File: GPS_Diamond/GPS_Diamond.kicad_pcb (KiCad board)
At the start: 4 copper layers, 20 x 20 mm, 36 parts, among them J1 CONN_01X04_MALE, J2 TEST_1P, J3 TEST_1P, J5 TEST_1P, J6 TEST_1P, U1 TCR2LE33LM, U2 STM32F042K6Ux, U3 SAM-M8Q, U4 FXOS8700CQ, U5 MS5637

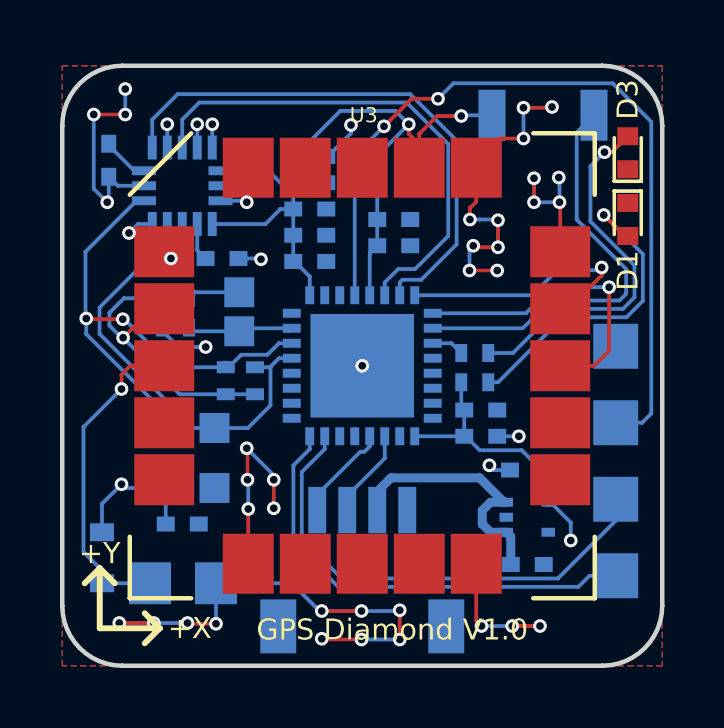
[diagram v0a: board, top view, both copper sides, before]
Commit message: Changed the boot0 jumper to a button and rearanged the baro.
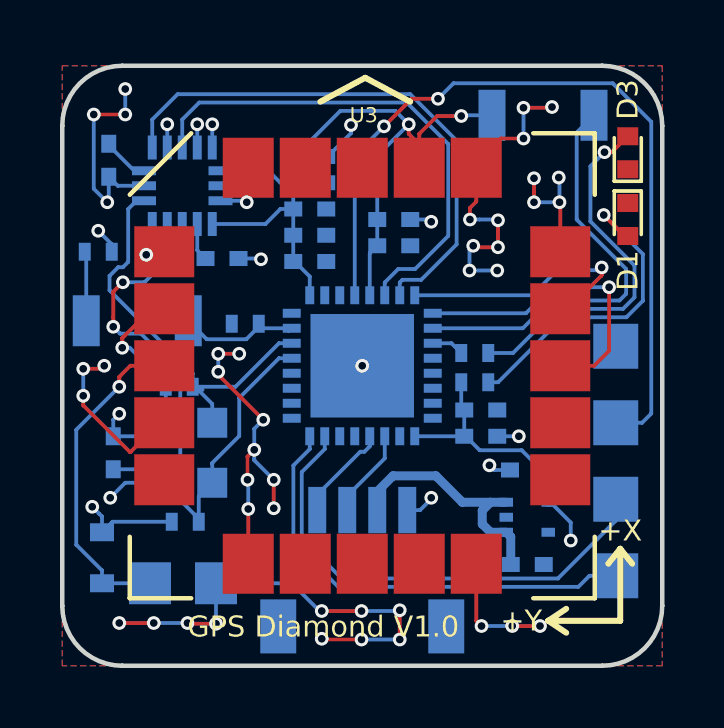
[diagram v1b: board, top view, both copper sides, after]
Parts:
- B1: footprint jumper:SOLDER-JUMPER_1-WAY -> Buttons_Switches_SMD:SW_SPST_B3U-1000P
- moved R6 5.24 mm to (144.1, 105.2), turned to 180 degrees
- moved B1 3.41 mm to (142.5, 98.5), turned to 0 degrees
- moved C11 3.31 mm to (141.7, 102.9), turned to 270 degrees
- moved R1 3.01 mm to (141.2, 96.2), turned to 180 degrees
- moved R7 2.33 mm to (146.1, 98.6)
- moved R8 1.56 mm to (143.9, 100.7), turned to 180 degrees
- moved U5 0.19 mm to (144.0, 102.9), turned to 270 degrees
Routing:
- net GND: track 58.0 -> 70.2 mm, vias 47 -> 55
- net I2C1_SCL: track 14.8 -> 19.9 mm, vias 0 -> 2
- net I2C1_SDA: track 17.8 -> 13.8 mm, vias 2 -> 0
- net +3V3: track 51.6 -> 48.8 mm, vias 5 -> 7
- net Net-(B1-Pad2): track 3.68 -> 4.25 mm
- net Net-(B1-Pad1): track 1.76 -> 2.32 mm
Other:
- board text added: "Boot0"

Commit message: Updates GPS Diamond to 1.1.
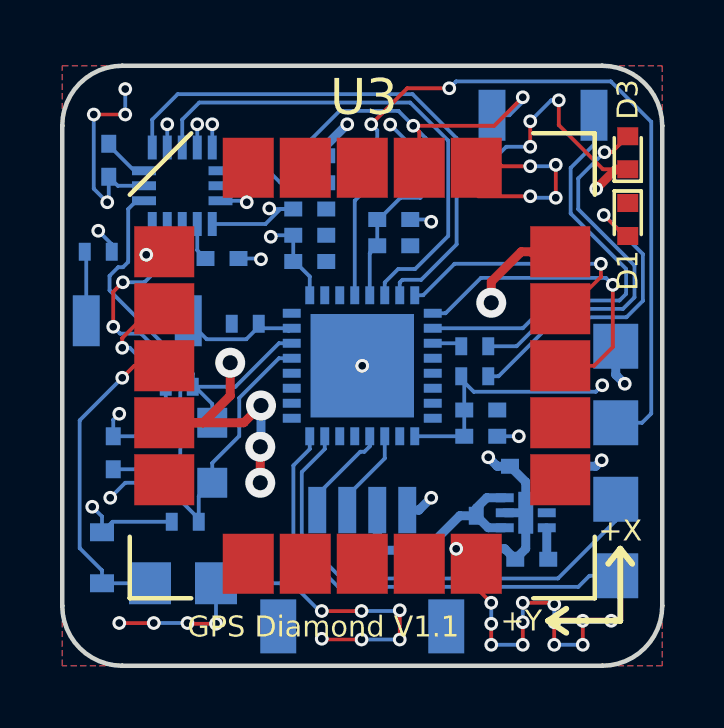
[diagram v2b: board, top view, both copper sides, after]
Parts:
- added C15: 100nF, Capacitors_SMD:C_0402, B.Cu at (151.1, 93.8)
- added C16: 1uF, Capacitors_SMD:C_0402, B.Cu at (153.8, 105.5)
- R6: value 10K -> 2k2
- R8: value 10K -> 2K2
- U1: value TCR2LE33LM -> MIC5353-3.3YMT-TR; footprint TO_SOT_Packages_SMD:SOT-553 -> local:MIC-5353
- moved C2 0.90 mm to (148.2, 93.0)
- moved C13 0.88 mm to (148.2, 93.9)
- moved C5 0.23 mm to (155.7, 106.5), turned to 180 degrees
- moved R4 0.23 mm to (153.8, 99.3)
- moved R3 0.20 mm to (153.8, 100.3)
- moved U1 0.16 mm to (155.4, 104.9), turned to 90 degrees
- moved C14 0.12 mm to (155.5, 103.3)
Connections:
- C5 pad 1: +5V -> Net-(C5-Pad1)
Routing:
- net GND: track 70.2 -> 84.2 mm
- net +3V3: track 48.8 -> 53.3 mm, vias 7 -> 10
- net Net-(C5-Pad1): track 0.00 -> 1.07 mm
- net +5V: track 8.39 -> 7.42 mm
- net USART2_TX: track 9.83 -> 8.87 mm
- net Net-(C15-Pad2): track 27.9 -> 28.4 mm
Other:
- net class Default: clearance 0.1524 -> 0.127
- net class Power: clearance 0.1524 -> 0.127
- rule pad_to_mask_clearance: 0.2 -> 0.125
- rule trace_clearance: 0.1524 -> 0.127
- board text added: "GPS Diamond V1.1"
- board text removed: "GPS Diamond V1.0"
